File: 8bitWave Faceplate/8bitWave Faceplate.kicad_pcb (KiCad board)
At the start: 2 copper layers, 99.7 x 64.1 mm, 13 parts, among them IC1 0.96_I2C_OLED, J1 I2C_VOL, J3 EXTENSION, M1 Mounting, M2 Mounting, M3 Mounting, M4 Mounting

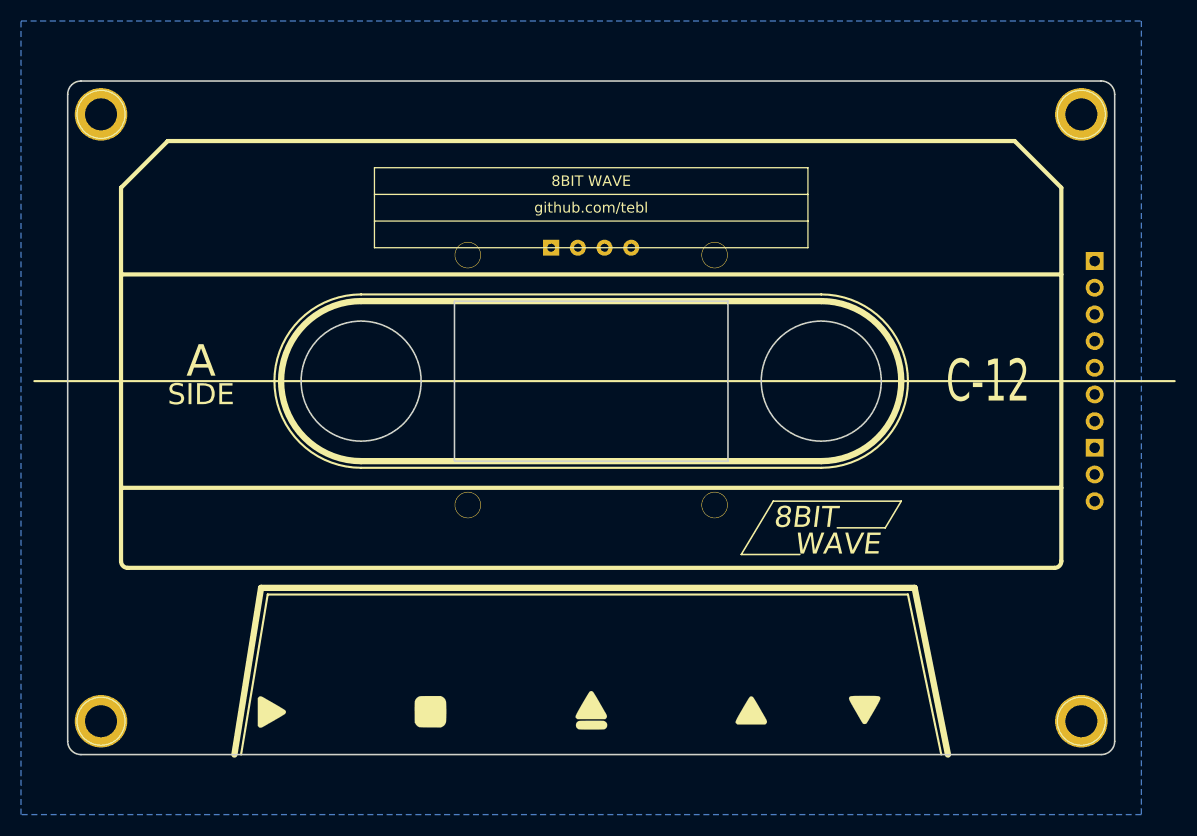
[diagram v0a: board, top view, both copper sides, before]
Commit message: Faceplate tracks routed
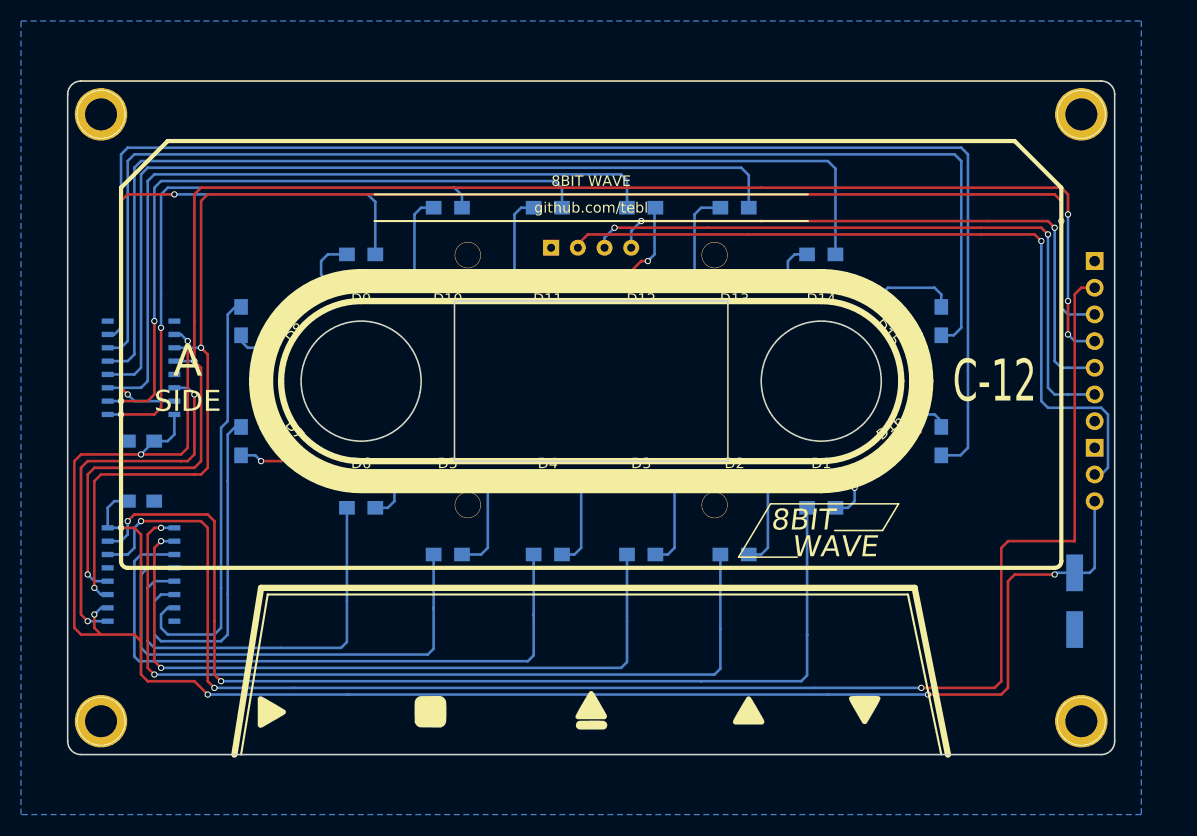
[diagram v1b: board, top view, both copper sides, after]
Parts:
- added C1: 100nF, Capacitors_SMD:C_0805_HandSoldering, B.Cu at (77.5, 118.1)
- added C2: 100nF, Capacitors_SMD:C_0805_HandSoldering, B.Cu at (77.5, 112.4)
- added C3: 10uF, Capacitors_SMD:CP_Elec_6.3x5.3, B.Cu at (166.4, 127.6)
- added D1: RED, LEDs:LED_0805_HandSoldering, F.Cu at (142.2, 116.2)
- added D10: RED, LEDs:LED_0805_HandSoldering, F.Cu at (106.7, 97.2)
- added D11: RED, LEDs:LED_0805_HandSoldering, F.Cu at (116.2, 97.2)
- added D12: RED, LEDs:LED_0805_HandSoldering, F.Cu at (125.1, 97.2)
- added D13: RED, LEDs:LED_0805_HandSoldering, F.Cu at (134.0, 97.2)
- added D14: RED, LEDs:LED_0805_HandSoldering, F.Cu at (142.2, 97.2)
- added D15: RED, LEDs:LED_0805_HandSoldering, F.Cu at (149.9, 101.0)
- added D16: RED, LEDs:LED_0805_HandSoldering, F.Cu at (149.9, 112.4)
- added D2: RED, LEDs:LED_0805_HandSoldering, F.Cu at (134.0, 116.2)
- added D3: RED, LEDs:LED_0805_HandSoldering, F.Cu at (125.1, 116.2)
- added D4: RED, LEDs:LED_0805_HandSoldering, F.Cu at (116.2, 116.2)
- added D5: RED, LEDs:LED_0805_HandSoldering, F.Cu at (106.7, 116.2)
- added D6: RED, LEDs:LED_0805_HandSoldering, F.Cu at (98.4, 116.2)
- added D7: RED, LEDs:LED_0805_HandSoldering, F.Cu at (90.8, 112.4)
- added D8: RED, LEDs:LED_0805_HandSoldering, F.Cu at (90.8, 101.0)
- added D9: RED, LEDs:LED_0805_HandSoldering, F.Cu at (98.4, 97.2)
- added R1: 330, Resistors_SMD:R_0805_HandSoldering, B.Cu at (142.2, 118.7)
- added R10: 330, Resistors_SMD:R_0805_HandSoldering, B.Cu at (106.7, 90.2)
- added R11: 330, Resistors_SMD:R_0805_HandSoldering, B.Cu at (116.2, 90.2)
- added R12: 330, Resistors_SMD:R_0805_HandSoldering, B.Cu at (125.1, 90.2)
- added R13: 330, Resistors_SMD:R_0805_HandSoldering, B.Cu at (134.0, 90.2)
- added R14: 330, Resistors_SMD:R_0805_HandSoldering, B.Cu at (142.2, 94.6)
- added R15: 330, Resistors_SMD:R_0805_HandSoldering, B.Cu at (153.7, 101.0)
- added R16: 330, Resistors_SMD:R_0805_HandSoldering, B.Cu at (153.7, 112.4)
- added R2: 330, Resistors_SMD:R_0805_HandSoldering, B.Cu at (134.0, 123.2)
- added R3: 330, Resistors_SMD:R_0805_HandSoldering, B.Cu at (125.1, 123.2)
- added R4: 330, Resistors_SMD:R_0805_HandSoldering, B.Cu at (116.2, 123.2)
- added R5: 330, Resistors_SMD:R_0805_HandSoldering, B.Cu at (106.7, 123.2)
- added R6: 330, Resistors_SMD:R_0805_HandSoldering, B.Cu at (98.4, 118.7)
- added R7: 330, Resistors_SMD:R_0805_HandSoldering, B.Cu at (87.0, 112.4)
- added R8: 330, Resistors_SMD:R_0805_HandSoldering, B.Cu at (87.0, 101.0)
- added R9: 330, Resistors_SMD:R_0805_HandSoldering, B.Cu at (98.4, 94.6)
- added U1: 74HC595_ALT, SMD_Packages:SO-16-N, B.Cu at (77.5, 125.1)
- added U2: 74HC595_ALT, SMD_Packages:SO-16-N, B.Cu at (77.5, 105.4)
- moved REF** 0.36 mm to (142.0, 119.9)
- moved G*** 0.25 mm to (135.1, 139.6)
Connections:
- J1 pad 3: (no net) -> +5V
- J3 pad 2: (no net) -> /SHIFT_DATA
- J3 pad 3: (no net) -> /SHIFT_CLOCK
- J3 pad 4: (no net) -> /SHIFT_LATCH
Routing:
- net +5V: track 0.00 -> 185.1 mm, vias 0 -> 7
- net /SHIFT_LATCH: track 0.00 -> 150.4 mm, vias 0 -> 5
- net /SHIFT_DATA: track 0.00 -> 148.5 mm, vias 0 -> 3
- net /SHIFT_CLOCK: track 0.00 -> 147.3 mm, vias 0 -> 3
- net Net-(R16-Pad1): track 0.00 -> 130.0 mm
- net Net-(R15-Pad1): track 0.00 -> 117.3 mm
- net Net-(R1-Pad1): track 0.00 -> 99.8 mm, vias 0 -> 2
- net Net-(R14-Pad1): track 0.00 -> 96.1 mm
- net Net-(R13-Pad1): track 0.00 -> 83.4 mm
- net Net-(R2-Pad1): track 0.00 -> 81.4 mm, vias 0 -> 2
- net VCC: track 0.00 -> 73.8 mm, vias 0 -> 1
- net Net-(R12-Pad1): track 0.00 -> 71.9 mm
- net Net-(R3-Pad1): track 0.00 -> 68.7 mm, vias 0 -> 2
- net Net-(R11-Pad1): track 0.00 -> 65.6 mm, vias 0 -> 2
- net /SCL: track 0.00 -> 63.1 mm, vias 0 -> 2
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
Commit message: Finishing touches
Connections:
- J1 pad 1: (no net) -> VCC
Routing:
- net VCC: track 73.8 -> 75.1 mm
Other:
- board text added: "8x 330"
- board text added: "8x LED"

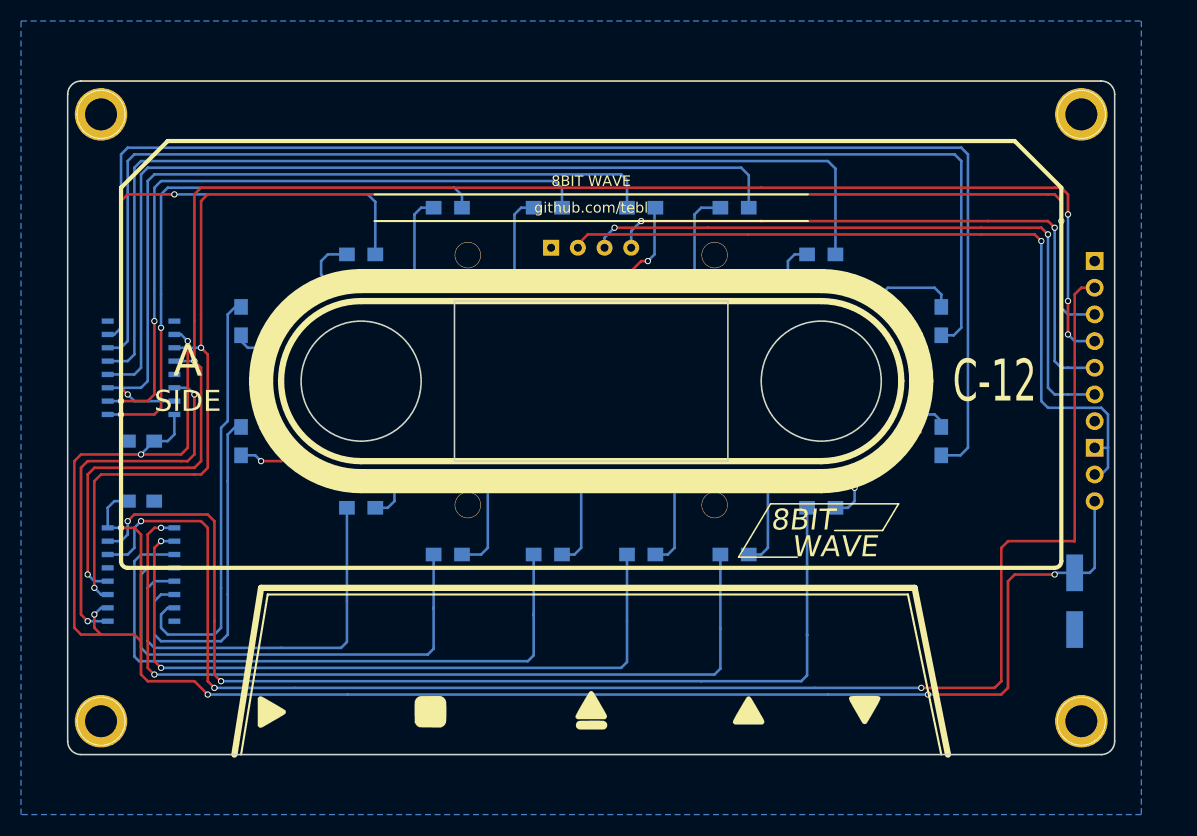
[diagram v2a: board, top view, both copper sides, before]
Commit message: Updated faceplate
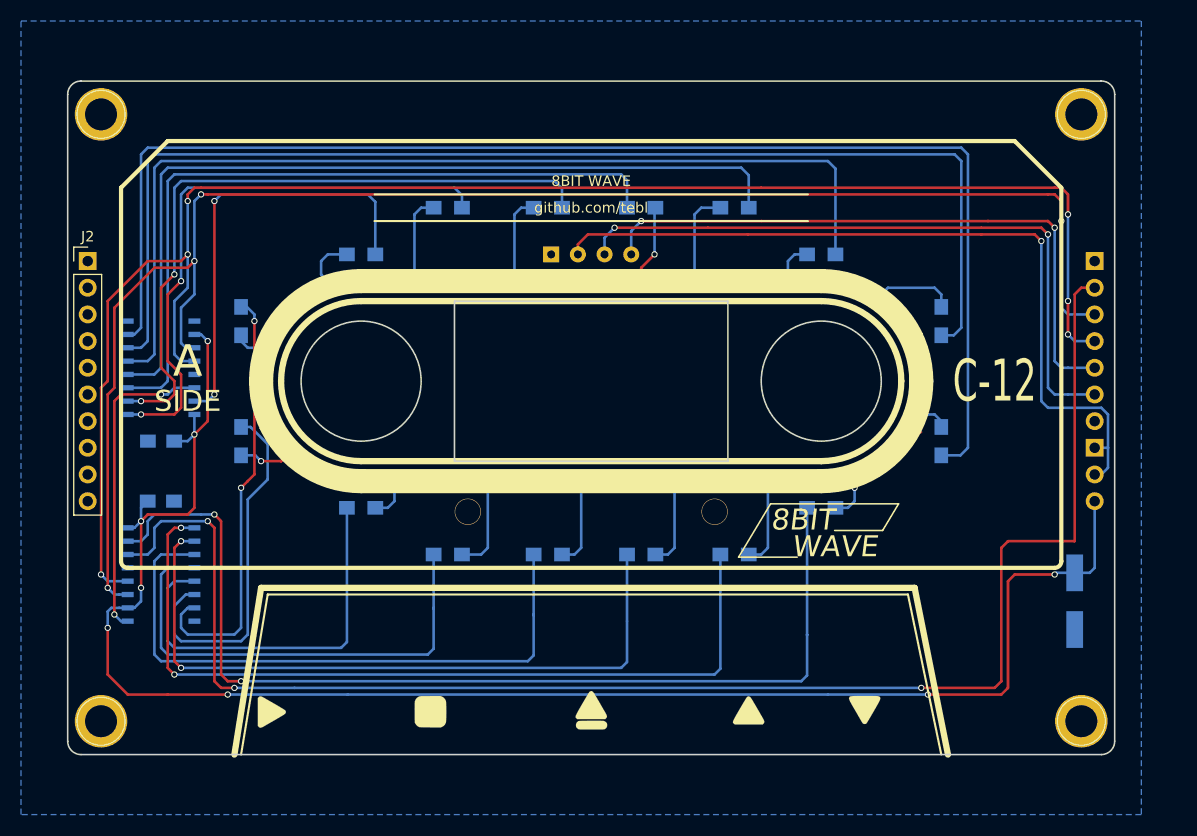
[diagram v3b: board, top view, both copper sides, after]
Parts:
- added J2: SPI, Pin_Headers:Pin_Header_Straight_1x10_Pitch2.54mm, F.Cu at (72.4, 95.2)
- moved C2 1.91 mm to (79.4, 112.4)
- moved U1 1.91 mm to (79.4, 125.1)
- moved U2 1.91 mm to (79.4, 105.4)
- moved C1 1.89 mm to (79.4, 118.1)
- moved IC1 0.63 mm to (120.3, 94.6)
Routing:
- net +5V: track 185.1 -> 160.6 mm, vias 7 -> 8
- net Net-(R9-Pad1): track 53.2 -> 41.5 mm
- net /SHIFT_LATCH: track 150.4 -> 157.0 mm, vias 5 -> 6
- net Net-(U1-Pad9): track 36.0 -> 30.0 mm
- net /SHIFT_CLOCK: track 147.3 -> 150.7 mm, vias 3 -> 4
- net Net-(R4-Pad1): track 61.3 -> 59.3 mm
- net Net-(R16-Pad1): track 130.0 -> 128.1 mm
- net Net-(R13-Pad1): track 83.4 -> 81.5 mm
- net Net-(R6-Pad1): track 40.1 -> 38.2 mm
- net Net-(R5-Pad1): track 47.8 -> 45.9 mm
- net Net-(R3-Pad1): track 68.7 -> 66.8 mm
- net Net-(R2-Pad1): track 81.4 -> 79.5 mm
- net Net-(R15-Pad1): track 117.3 -> 115.4 mm
- net Net-(R12-Pad1): track 71.9 -> 70.0 mm
- net Net-(R1-Pad1): track 99.8 -> 97.9 mm
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
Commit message: Gerber export
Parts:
- moved C3 21.0 mm to (145.4, 128.9), turned to 90 degrees
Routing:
- net +5V: track 160.6 -> 160.1 mm
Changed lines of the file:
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@@
     (thickness 1.6)
     (drawings 59)
-    (tracks 485)
+    (tracks 489)
     (zones 0)
     (modules 51)
@@
   )
   (module Capacitors_SMD:CP_Elec_6.3x5.3 (layer B.Cu)
-    (at 166.37 127.635 270)
+    (at 145.415 128.905 90)
     (descr "SMT capacitor, aluminium electrolytic, 6.3x5.3")
     (attr smd)
@@
     (fp_line (start 4.7 -3.4) (end 4.7 3.4) (layer B.CrtYd) (width 0.05))
     (fp_line (start 4.7 -3.4) (end -4.7 -3.4) (layer B.CrtYd) (width 0.05))
-    (pad 1 smd rect (at -2.7 0 90) (size 3.5 1.6) (layers B.Cu B.Paste B.Mask)
+    (pad 1 smd rect (at -2.7 0 270) (size 3.5 1.6) (layers B.Cu B.Paste B.Mask)
       (net 5 +5V))
-    (pad 2 smd rect (at 2.7 0 90) (size 3.5 1.6) (layers B.Cu B.Paste B.Mask)
+    (pad 2 smd rect (at 2.7 0 270) (size 3.5 1.6) (layers B.Cu B.Paste B.Mask)
       (net 1 GND))
     (model Capacitors_SMD.3dshapes/CP_Elec_6.3x5.3.wrl
@@
   (segment (start 119.065 93.98) (end 119.065 93.66) (width 0.25) (layer F.Cu) (net 4))
   (segment (start 166.37 124.935) (end 164.625 124.935) (width 0.25) (layer B.Cu) (net 5))
-  (via (at 152.4 136.525) (size 0.6) (drill 0.4) (layers F.Cu B.Cu) (net 5))
-  (segment (start 152.4 136.525) (end 159.385 136.525) (width 0.25) (layer F.Cu) (net 5))
-  (segment (start 159.385 136.525) (end 160.02 135.89) (width 0.25) (layer F.Cu) (net 5))
-  (segment (start 160.02 135.89) (end 160.02 125.73) (width 0.25) (layer F.Cu) (net 5))
   (segment (start 142.875 136.525) (end 97.155 136.525) (width 0.25) (layer B.Cu) (net 5))
   (via (at 85.725 136.525) (size 0.6) (drill 0.4) (layers F.Cu B.Cu) (net 5))
-  (segment (start 142.875 136.525) (end 152.4 136.525) (width 0.25) (layer B.Cu) (net 5))
-  (segment (start 160.655 125.095) (end 160.02 125.73) (width 0.25) (layer F.Cu) (net 5))
   (segment (start 164.465 125.095) (end 160.655 125.095) (width 0.25) (layer F.Cu) (net 5))
   (via (at 164.465 125.095) (size 0.6) (drill 0.4) (layers F.Cu B.Cu) (net 5))
@@
   (segment (start 83.82 102.87) (end 83.185 102.235) (width 0.25) (layer B.Cu) (net 5))
   (segment (start 83.185 102.235) (end 82.55 102.235) (width 0.25) (layer B.Cu) (net 5))
+  (segment (start 145.415 135.89) (end 144.78 136.525) (width 0.25) (layer B.Cu) (net 5))
+  (segment (start 142.875 136.525) (end 144.78 136.525) (width 0.25) (layer B.Cu) (net 5))
+  (segment (start 145.415 131.605) (end 145.415 135.89) (width 0.25) (layer B.Cu) (net 5))
+  (segment (start 147.32 130.75) (end 147.32 130.175) (width 0.25) (layer B.Cu) (net 5))
+  (segment (start 145.415 131.605) (end 146.465 131.605) (width 0.25) (layer B.Cu) (net 5))
+  (via (at 147.32 130.175) (size 0.6) (drill 0.4) (layers F.Cu B.Cu) (net 5))
+  (segment (start 146.465 131.605) (end 147.32 130.75) (width 0.25) (layer B.Cu) (net 5))
+  (segment (start 147.32 130.175) (end 147.32 125.73) (width 0.25) (layer F.Cu) (net 5))
+  (segment (start 147.955 125.095) (end 160.655 125.095) (width 0.25) (layer F.Cu) (net 5))
+  (segment (start 147.32 125.73) (end 147.955 125.095) (width 0.25) (layer F.Cu) (net 5))
   (segment (start 143.59 116.205) (end 144.78 116.205) (width 0.25) (layer F.Cu) (net 6))
   (segment (start 144.78 118.745) (end 143.59 118.745) (width 0.25) (layer B.Cu) (net 6))
@@
   (via (at 137.16 116.84) (size 0.6) (drill 0.4) (layers F.Cu B.Cu) (net 7))
   (segment (start 136.525 116.205) (end 137.16 116.84) (width 0.25) (layer F.Cu) (net 7))
-  (segment (start 159.385 122.555) (end 160.02 121.92) (width 0.25) (layer F.Cu) (net 8))
   (segment (start 166.37 98.425) (end 167.005 97.79) (width 0.25) (layer F.Cu) (net 8))
   (segment (start 166.37 121.92) (end 166.37 98.425) (width 0.25) (layer F.Cu) (net 8))
@@
   (via (at 86.36 135.89) (size 0.6) (drill 0.4) (layers F.Cu B.Cu) (net 8))
   (segment (start 167.005 97.79) (end 168.275 97.79) (width 0.25) (layer F.Cu) (net 8))
-  (segment (start 159.385 135.255) (end 159.385 122.555) (width 0.25) (layer F.Cu) (net 8))
-  (segment (start 158.75 135.89) (end 159.385 135.255) (width 0.25) (layer F.Cu) (net 8))
-  (segment (start 151.765 135.89) (end 158.75 135.89) (width 0.25) (layer F.Cu) (net 8))
-  (via (at 151.765 135.89) (size 0.6) (drill 0.4) (layers F.Cu B.Cu) (net 8))
   (segment (start 92.075 135.89) (end 86.36 135.89) (width 0.25) (layer B.Cu) (net 8))
-  (segment (start 151.765 135.89) (end 92.075 135.89) (width 0.25) (layer B.Cu) (net 8))
   (via (at 83.82 120.015) (size 0.6) (drill 0.4) (layers F.Cu B.Cu) (net 8))
   (segment (start 83.82 120.015) (end 79.375 120.015) (width 0.25) (layer B.Cu) (net 8))
@@
   (segment (start 84.455 135.255) (end 85.09 135.89) (width 0.25) (layer F.Cu) (net 8))
   (segment (start 86.36 135.89) (end 85.09 135.89) (width 0.25) (layer F.Cu) (net 8))
+  (segment (start 160.02 121.92) (end 142.24 121.92) (width 0.25) (layer F.Cu) (net 8))
+  (segment (start 142.24 121.92) (end 141.605 122.555) (width 0.25) (layer F.Cu) (net 8))
+  (segment (start 141.605 122.555) (end 141.605 135.255) (width 0.25) (layer F.Cu) (net 8))
+  (segment (start 141.605 135.255) (end 140.97 135.89) (width 0.25) (layer F.Cu) (net 8))
+  (via (at 140.97 135.89) (size 0.6) (drill 0.4) (layers F.Cu B.Cu) (net 8))
+  (segment (start 140.97 135.89) (end 92.075 135.89) (width 0.25) (layer B.Cu) (net 8))
   (segment (start 165.1 99.695) (end 165.1 91.44) (width 0.25) (layer B.Cu) (net 9))
   (via (at 165.1 91.44) (size 0.6) (drill 0.4) (layers F.Cu B.Cu) (net 9))
